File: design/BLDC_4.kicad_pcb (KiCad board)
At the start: 4 copper layers, 38.5 x 65 mm, 129 parts, among them K1 SERVO, P1 HALL/Encoder, P101 CANBUS, P2 SWD, P3 PWR_COMM, P4 IN+, P5 IN-, P6 MOTOR1, P7 MOTOR2, P9 MOTOR3, Q1 IRFS7530, Q2 IRFS7530, Q3 IRFS7530, Q4 IRFS7530, Q5 IRFS7530, Q6 IRFS7530, U1 STM32F40X_LQFP64, U2 TC2117, U3 DRV8302, U401 SN65HVD232, X1 MINI-USB-SHIELD-32005-201, X2 8MHz 10ppm

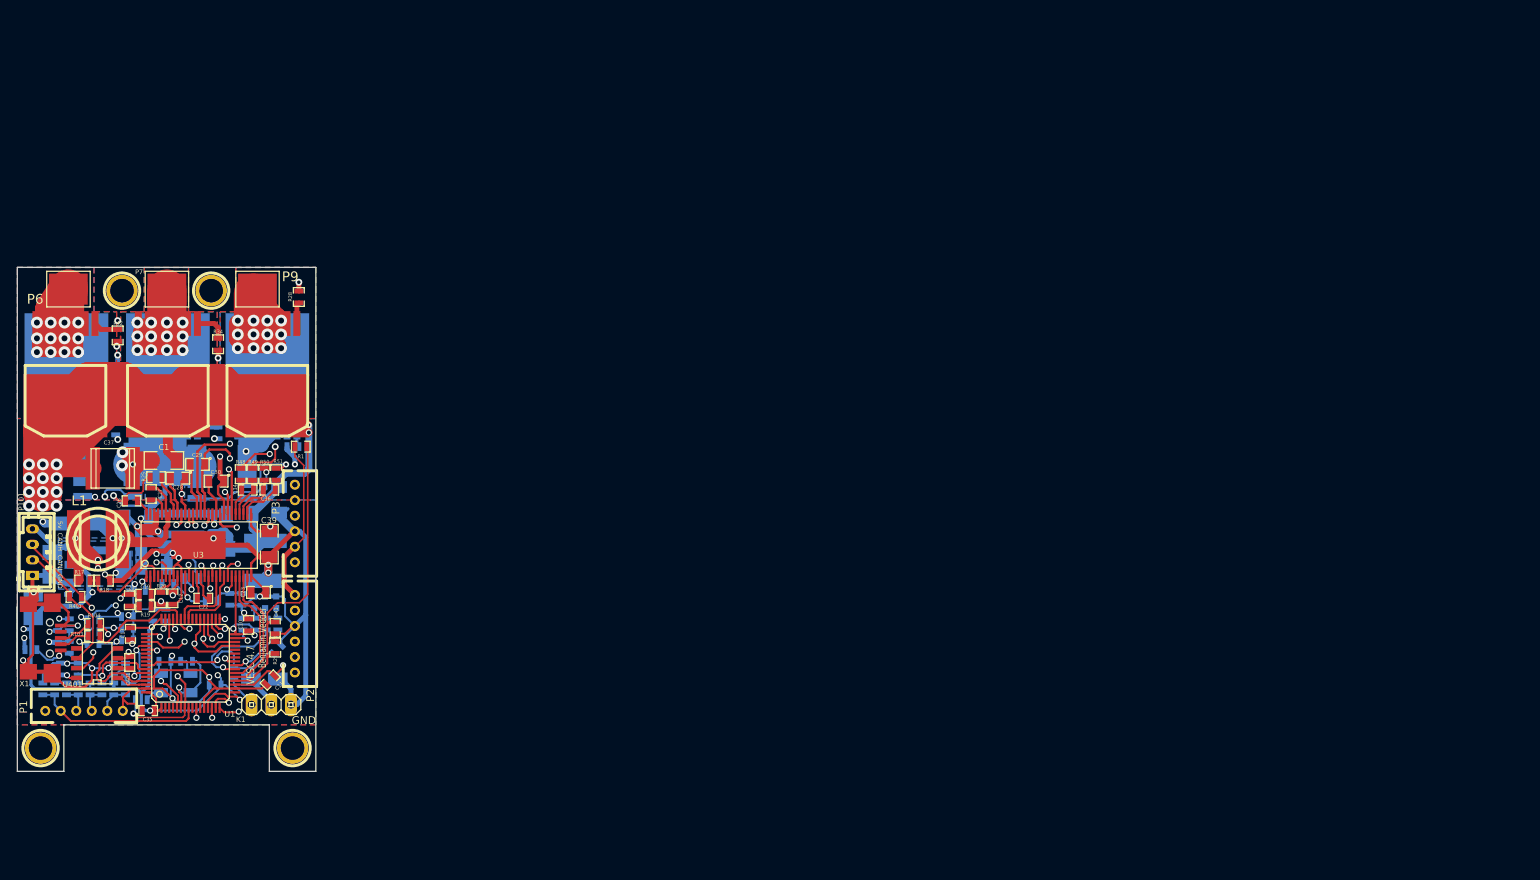
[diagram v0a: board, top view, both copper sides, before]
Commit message: Generated first netlist and started working with pcbnew.
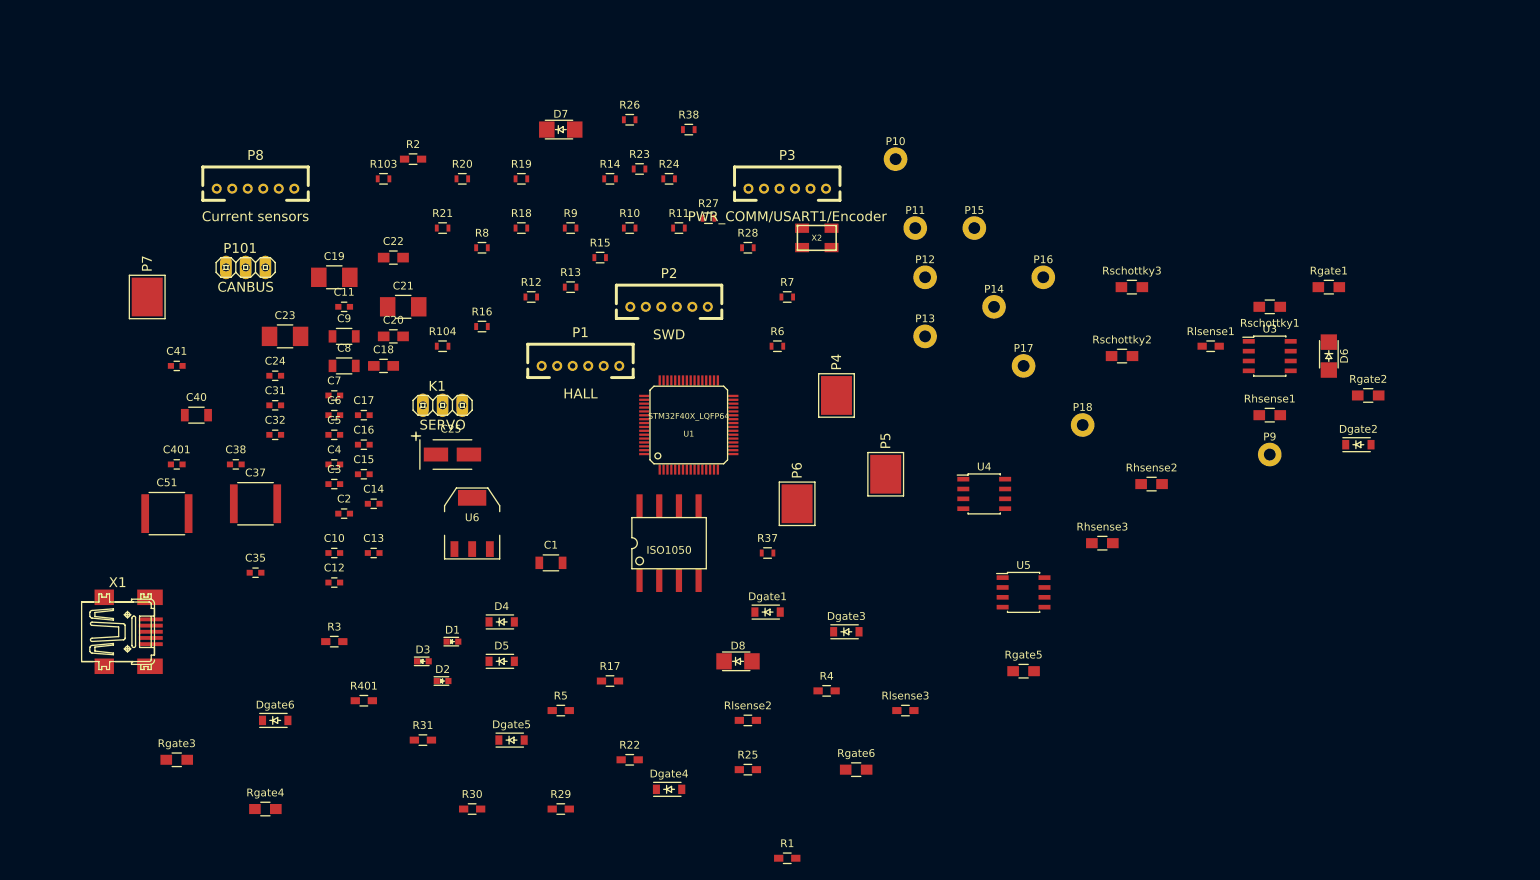
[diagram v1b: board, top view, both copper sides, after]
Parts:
- removed 1PIN (x2): P***, 1pin
- removed 1PIN (x2): P***, Connect:1pin
- removed C26: 15n, SMD_Packages:SMD-0603_c
- removed C27: 100n, SMD_Packages:SMD-0603_c
- removed C28, C29, C30: 220n, SMD_Packages:SMD-0805
- removed C33: 100u, w_smd_cap:c_tant_B
- removed C34, C36: 2.2n, SMD_Packages:SMD-0603_c
- removed C39, C43, C44, C49: 10u,50V, SMD_Packages:SMD-1206
- removed C52: 2.2u, SMD_Packages:SMD-0603_c
- removed G***: oshw_silkscreen-back_3mm, oshw_silkscreen-back_3mm
- removed L1: 22u, w_smd_inductors:inductor_smd_8x5mm
- removed Q1, Q2, Q3, Q4, Q5, Q6: IRFS7530, CRF1:D2PAK-7-GDS
- removed R32, R36, R46: 39k, SMD_Packages:SMD-0603_r
- removed R33: 2k2, SMD_Packages:SMD-0603_r
- removed R34, R35, R42, R43: 4R7, SMD_Packages:SMD-0603_r
- removed R402: 10k, SMD_Packages:SMD-0603_r
- removed R48, R49, R50, R51: 100R, SMD_Packages:SMD-0603_r
- removed R53, R54: SHUNT, CRF1:WSLP2726
- removed U401: SN65HVD232, SMD_Packages:SOIC-8-W
- added D6: D_Schottky, FootprintsBLDC:DO-214AC_SOD-123, F.Cu at (247.7, 91.4)
- added D7: D_Schottky, FootprintsBLDC:DO-214AC_SOD-123, F.Cu at (148.6, 62.2)
- added D8: D_Schottky, FootprintsBLDC:DO-214AC_SOD-123, F.Cu at (171.4, 130.8)
- added Dgate1: D, Diodes_SMD:SOD-123, F.Cu at (175.3, 124.5)
- added Dgate2: D, Diodes_SMD:SOD-123, F.Cu at (251.5, 102.9)
- added Dgate3: D, Diodes_SMD:SOD-123, F.Cu at (185.4, 127.0)
- added Dgate4: D, Diodes_SMD:SOD-123, F.Cu at (162.6, 147.3)
- added Dgate5: D, Diodes_SMD:SOD-123, F.Cu at (142.2, 141.0)
- added Dgate6: D, Diodes_SMD:SOD-123, F.Cu at (111.8, 138.4)
- added P10: CONN_DRV, FootprintsBLDC:PAD_DRV, F.Cu at (191.8, 66.0)
- added P11: CONN_DRV, FootprintsBLDC:PAD_DRV, F.Cu at (194.3, 74.9)
- added P12: CONN_DRV, FootprintsBLDC:PAD_DRV, F.Cu at (195.6, 81.3)
- added P13: CONN_DRV, FootprintsBLDC:PAD_DRV, F.Cu at (195.6, 88.9)
- added P14: CONN_DRV, FootprintsBLDC:PAD_DRV, F.Cu at (204.5, 85.1)
- added P15: CONN_DRV, FootprintsBLDC:PAD_DRV, F.Cu at (201.9, 74.9)
- added P16: CONN_DRV, FootprintsBLDC:PAD_DRV, F.Cu at (210.8, 81.3)
- added P17: CONN_DRV, FootprintsBLDC:PAD_DRV, F.Cu at (208.3, 92.7)
- added P18: CONN_DRV, FootprintsBLDC:PAD_DRV, F.Cu at (215.9, 100.3)
- added P8: Current sensors, CRF1:MICRO_JST_6, F.Cu at (109.2, 69.8)
- added R14: 100, Resistors_SMD:R_0603, F.Cu at (154.9, 68.6)
- added R31: R, Resistors_SMD:R_0603_HandSoldering, F.Cu at (130.8, 141.0)
- added Rgate1: 4.7, Resistors_SMD:R_0805_HandSoldering, F.Cu at (247.7, 82.5)
- added Rgate2: 4.7, Resistors_SMD:R_0805_HandSoldering, F.Cu at (252.7, 96.5)
- added Rgate3: 4.7, Resistors_SMD:R_0805_HandSoldering, F.Cu at (99.1, 143.5)
- added Rgate4: 4.7, Resistors_SMD:R_0805_HandSoldering, F.Cu at (110.5, 149.9)
- added Rgate5: 4.7, Resistors_SMD:R_0805_HandSoldering, F.Cu at (208.3, 132.1)
- added Rgate6: 4.7, Resistors_SMD:R_0805_HandSoldering, F.Cu at (186.7, 144.8)
- added Rhsense1: R, Resistors_SMD:R_0805_HandSoldering, F.Cu at (240.0, 99.1)
- added Rhsense2: R, Resistors_SMD:R_0805_HandSoldering, F.Cu at (224.8, 108.0)
- added Rhsense3: R, Resistors_SMD:R_0805_HandSoldering, F.Cu at (218.4, 115.6)
- added Rlsense1: R, Resistors_SMD:R_0603_HandSoldering, F.Cu at (232.4, 90.2)
- added Rlsense2: R, Resistors_SMD:R_0603_HandSoldering, F.Cu at (172.7, 138.4)
- added Rlsense3: R, Resistors_SMD:R_0603_HandSoldering, F.Cu at (193.0, 137.2)
- added Rschottky1: 2.7, Resistors_SMD:R_0805_HandSoldering, F.Cu at (240.0, 85.1)
- added Rschottky2: 2.7, Resistors_SMD:R_0805_HandSoldering, F.Cu at (221.0, 91.4)
- added Rschottky3: 2.7, Resistors_SMD:R_0805_HandSoldering, F.Cu at (222.2, 82.5)
- added U4: IRS2184, Housings_SOIC:SOIC-8_3.9x4.9mm_Pitch1.27mm, F.Cu at (203.2, 109.2)
- added U5: IRS2184, Housings_SOIC:SOIC-8_3.9x4.9mm_Pitch1.27mm, F.Cu at (208.3, 121.9)
- added U6: NCP1117ST33T3G, TO_SOT_Packages_SMD:SOT-223, F.Cu at (137.2, 113.0)
- C1: footprint SMD_Packages:SMD-1206 -> Capacitors_SMD:C_1206
- C10, C11, C12, C13, C35, C41: footprint SMD_Packages:SMD-0603_c -> Capacitors_SMD:C_0603
- C14, C15, C16, C17, C2, C24, C3, C31, C32, C38, C4, C5, C6, C7: footprint SMD_Packages:SMD-0603_c -> Capacitors_SMD:C_0603; moved to F.Cu
- C18: value 2.2u -> 0.47uF; footprint SMD_Packages:SMD-0805 -> Capacitors_SMD:C_0805_HandSoldering; moved to F.Cu
- C19: value 120p -> 1uF; footprint SMD_Packages:SMD-0603_c -> Capacitors_SMD:C_1210_HandSoldering
- C20: value 2.2u -> 0.47uF; footprint SMD_Packages:SMD-0603_c -> Capacitors_SMD:C_0805_HandSoldering; moved to F.Cu
- C21: value 6.8n -> 1uF; footprint SMD_Packages:SMD-0603_c -> Capacitors_SMD:C_1210_HandSoldering
- C22: value 22n -> 0.47uF; footprint SMD_Packages:SMD-0603_c -> Capacitors_SMD:C_0805_HandSoldering
- C23: value 2.2u -> 1uF; footprint SMD_Packages:SMD-0805 -> Capacitors_SMD:C_1210_HandSoldering
- C25: footprint w_smd_cap:c_tant_B -> Capacitors_Tantalum_SMD:TantalC_SizeB_EIA-3528_HandSoldering; moved to F.Cu
- C37: footprint w_smd_cap:c_2220 -> Capacitors_SMD:C_2220
- C40, C8, C9: footprint SMD_Packages:SMD-1206 -> Capacitors_SMD:C_1206; moved to F.Cu
- C401: footprint SMD_Packages:SMD-0603 -> Capacitors_SMD:C_0603
- C51: footprint w_smd_cap:c_2220 -> Capacitors_SMD:C_2220; moved to F.Cu
- D1, D2, D3, P4, P5, X2: moved to F.Cu
- D4: value DIODESCH -> BAT46WH; footprint Diodes_SMD:Diode-SMA_Handsoldering -> Diodes_SMD:SOD-123; moved to F.Cu
- D5: value TVS 5V -> BAT46WH; footprint w_smd_diode:do214ac -> Diodes_SMD:SOD-123; moved to F.Cu
- P1: value HALL/Encoder -> HALL
- P101: footprint JST conn:b4b-ph-kl -> CRF1:pinhead-1X03
- P3: value PWR_COMM -> PWR_COMM/USART1/Encoder
- P6: value MOTOR1 -> CONN_DRV
- P7: value MOTOR2 -> CONN_DRV
- P9: value MOTOR3 -> CONN_DRV; footprint CRF1:1PAD_4x5mm -> FootprintsBLDC:PAD_DRV
- R1, R2, R401: footprint SMD_Packages:SMD-0603_r -> Resistors_SMD:R_0603_HandSoldering
- R10, R11, R12, R13, R37, R38, R7, R8, R9: footprint SMD_Packages:SMD-0603_r -> Resistors_SMD:R_0603; moved to F.Cu
- R103, R104: footprint SMD_Packages:SMD-0603_r -> Resistors_SMD:R_0603
- R15: value 330k -> 100; footprint SMD_Packages:SMD-0603_r -> Resistors_SMD:R_0603; moved to F.Cu
- R16: value 10k -> 100; footprint SMD_Packages:SMD-0603_r -> Resistors_SMD:R_0603; moved to F.Cu
- R17: value 18k -> 0R; footprint SMD_Packages:SMD-0603_r -> Resistors_SMD:R_0603_HandSoldering
- R18: value 3k3 -> 1k; footprint SMD_Packages:SMD-0603_r -> Resistors_SMD:R_0603
- R19: value 15k -> 1k; footprint SMD_Packages:SMD-0603_r -> Resistors_SMD:R_0603
- R20: value 10k -> 1k; footprint SMD_Packages:SMD-0603_r -> Resistors_SMD:R_0603
- R21: value 220k -> 1k; footprint SMD_Packages:SMD-0603_r -> Resistors_SMD:R_0603; moved to F.Cu
- R22, R3, R4, R5: footprint SMD_Packages:SMD-0603_r -> Resistors_SMD:R_0603_HandSoldering; moved to F.Cu
- R23: value 39k -> 1k; footprint SMD_Packages:SMD-0603_r -> Resistors_SMD:R_0603; moved to F.Cu
- R24: value 2k2 -> 1k; footprint SMD_Packages:SMD-0603_r -> Resistors_SMD:R_0603; moved to F.Cu
- R25: value 1M -> 0R/DNP; footprint SMD_Packages:SMD-0603_r -> Resistors_SMD:R_0603_HandSoldering
- R26: value 39k -> R; footprint SMD_Packages:SMD-0603_r -> Resistors_SMD:R_0603; moved to F.Cu
- R27: value 2k2 -> R; footprint SMD_Packages:SMD-0603_r -> Resistors_SMD:R_0603; moved to F.Cu
- R28: value 4R7 -> R; footprint SMD_Packages:SMD-0603_r -> Resistors_SMD:R_0603
- R29: value 4R7 -> R; footprint SMD_Packages:SMD-0603_r -> Resistors_SMD:R_0603_HandSoldering; moved to F.Cu
- R30: value 39k -> R; footprint SMD_Packages:SMD-0603_r -> Resistors_SMD:R_0603_HandSoldering; moved to F.Cu
- R6: value 0R -> 10k; footprint SMD_Packages:SMD-0603_r -> Resistors_SMD:R_0603; moved to F.Cu
- U2: value TC2117 -> ISO1050; footprint SMD_Packages:SOT-223 -> CRF1:PDSO-G8; moved to F.Cu
- U3: value DRV8302 -> IRS2184; footprint CRF1:TSSOP-56-PP -> Housings_SOIC:SOIC-8_3.9x4.9mm_Pitch1.27mm
- X1: footprint Mrk Industries:USB-UX60R-MB-5ST -> CRF1:con-cypressindustries-32005-201
- moved U3 140.3 mm to (240.0, 91.4)
- moved P9 132.3 mm to (240.0, 104.1), turned to 0 degrees
- moved R7 107.2 mm to (177.8, 83.8), turned to 0 degrees
- moved R6 103.9 mm to (176.5, 90.2), turned to 0 degrees
- moved P4 103.1 mm to (184.2, 96.5)
- moved X2 100.7 mm to (181.6, 76.2)
- moved P6 98.0 mm to (179.1, 110.5), turned to 0 degrees
- moved R4 97.8 mm to (182.9, 134.6), turned to 0 degrees
- moved R26 95.7 mm to (157.5, 61.0)
- moved R11 94.1 mm to (163.8, 74.9), turned to 0 degrees
- moved R23 93.4 mm to (158.8, 67.3)
- moved P5 93.0 mm to (190.5, 106.7)
- moved R24 91.7 mm to (162.6, 68.6), turned to 0 degrees
- moved R27 91.7 mm to (167.6, 73.7), turned to 0 degrees
- moved R10 88.1 mm to (157.5, 74.9), turned to 0 degrees
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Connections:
- C18 pad 1: Net-(C18-Pad1) -> V_SUPPLY
- C19 pad 1: GND -> Net-(C19-Pad1)
- C19 pad 2: Net-(C19-Pad2) -> /Half Bridge Driver U/VS
- C20 pad 1: GND -> V_SUPPLY
- C20 pad 2: Net-(C20-Pad2) -> GND
- C21 pad 1: GND -> Net-(C21-Pad1)
- C21 pad 2: Net-(C21-Pad2) -> /Half Bridge Driver V/VS
- C22 pad 1: Net-(C22-Pad1) -> V_SUPPLY
- C22 pad 2: Net-(C22-Pad2) -> GND
- C23 pad 1: GND -> Net-(C23-Pad1)
- C23 pad 2: Net-(C23-Pad2) -> /Half Bridge Driver W/VS
- C31 pad 2: VCC -> Net-(C31-Pad2)
- C35 pad 2: VCC -> Net-(C31-Pad2)
- D4 pad 1: GND -> V_SUPPLY
- D4 pad 2: Net-(C27-Pad1) -> Net-(D4-Pad2)
- D5 pad 1: GND -> V_SUPPLY
- D5 pad 2: +5V -> Net-(D5-Pad2)
- K1 pad 2: +5V -> Net-(D5-Pad2)
- P1 pad 1: +5V -> /Filters/TEMP_IN
- P1 pad 2: /Filters/TEMP_IN -> /Filters/HALL1_IN
- P1 pad 3: /Filters/HALL1_IN -> /Filters/HALL2_IN
- P1 pad 4: /Filters/HALL2_IN -> /Filters/HALL3_IN
- P1 pad 5: /Filters/HALL3_IN -> GND
- P1 pad 6: GND -> VCC
- P101 pad 1: GND -> /CAN bus transceiver/CANGND
- P2 pad 6: Net-(P2-Pad6) -> (no net)
- P3 pad 3: /MCU/ADC_EXT -> Net-(P3-Pad3)
- P3 pad 4: GND -> Net-(P3-Pad4)
- P3 pad 5: VCC -> GND
- P3 pad 6: +5V -> VCC
- P6 pad 1: /Mosfet driver/H3_VS -> /Half Bridge Driver U/HO
- P7 pad 1: /Mosfet driver/H2_VS -> /Half Bridge Driver U/VS
- P9 pad 1: /Mosfet driver/H1_VS -> /Half Bridge Driver U/LO
- R15 pad 1: Net-(C20-Pad2) -> /MCU/USART1_TX
- R15 pad 2: Net-(R15-Pad2) -> Net-(P3-Pad4)
- R16 pad 1: Net-(R15-Pad2) -> /MCU/ADC_EXT
- R16 pad 2: GND -> Net-(P8-Pad4)
- R17 pad 1: +5V -> VCC
- R17 pad 2: Net-(R17-Pad2) -> Net-(C31-Pad2)
- R18 pad 1: Net-(R17-Pad2) -> Net-(R18-Pad1)
- R18 pad 2: GND -> /Half Bridge Driver U/DRV_IN
- R19 pad 1: Net-(C21-Pad2) -> Net-(R19-Pad1)
- R19 pad 2: Net-(C19-Pad2) -> /Half Bridge Driver U/DRV_SD
- R20 pad 2: GND -> /Half Bridge Driver V/DRV_IN
- R21 pad 1: GND -> Net-(R21-Pad1)
- R21 pad 2: Net-(R21-Pad2) -> /Half Bridge Driver V/DRV_SD
- R23 pad 1: /Mosfet driver/H3_VS -> Net-(R23-Pad1)
- R23 pad 2: /MCU/SENS1 -> /Half Bridge Driver W/DRV_IN
- R24 pad 1: GND -> Net-(R24-Pad1)
- R24 pad 2: /MCU/SENS1 -> /Half Bridge Driver W/DRV_SD
- R25 pad 1: GND -> VCC
- R25 pad 2: Net-(R25-Pad2) -> /IF-Current/V_SUPPLY
- R26 pad 1: /Mosfet driver/H2_VS -> /MCU/CURR1
- R26 pad 2: /MCU/SENS2 -> /IF-Current/CURR1_IN
- R27 pad 1: GND -> /MCU/CURR2
- R27 pad 2: /MCU/SENS2 -> /IF-Current/CURR2_IN
- R28 pad 1: Net-(Q1-PadG) -> /MCU/CURR3
- R28 pad 2: /Mosfet driver/M_H1 -> /IF-Current/CURR3_IN
- R29 pad 1: Net-(Q2-PadG) -> /MCU/SENSY
- R29 pad 2: /Mosfet driver/M_L1 -> /MCU/SENS1
- R30 pad 1: /Mosfet driver/H1_LOW -> /MCU/SENSY
- R30 pad 2: Net-(Q2-PadG) -> /MCU/SENS2
- R6 pad 1: Net-(R6-Pad1) -> Net-(D4-Pad2)
- R6 pad 2: +5V -> GND
- U1 pad 11: Net-(U1-Pad11) -> (no net)
- U1 pad 13: VCC -> Net-(C31-Pad2)
- U1 pad 17: Net-(U1-Pad17) -> /MCU/SENSY
- U1 pad 2: Net-(U1-Pad2) -> (no net)
- U1 pad 20: /MCU/ADC_TEMP -> /MCU/CURR3
- U1 pad 21: /MCU/BR_SO2 -> /MCU/CURR2
- U1 pad 22: /MCU/BR_SO1 -> /MCU/CURR1
- U1 pad 26: Net-(U1-Pad26) -> (no net)
- U1 pad 27: Net-(U1-Pad27) -> (no net)
- U1 pad 28: Net-(U1-Pad28) -> (no net)
- U1 pad 3: Net-(U1-Pad3) -> (no net)
- U1 pad 33: /MCU/DC_CAL -> (no net)
- U1 pad 34: /MCU/L3 -> /Half Bridge Driver W/DRV_SD
- U1 pad 35: /MCU/L2 -> /Half Bridge Driver V/DRV_SD
- U1 pad 36: /MCU/L1 -> /Half Bridge Driver U/DRV_SD
- U1 pad 39: Net-(U1-Pad39) -> (no net)
- U1 pad 4: Net-(U1-Pad4) -> (no net)
- U1 pad 40: Net-(U1-Pad40) -> (no net)
- U1 pad 41: /MCU/H3 -> /Half Bridge Driver W/DRV_IN
- U1 pad 42: /MCU/H2 -> /Half Bridge Driver V/DRV_IN
- U1 pad 43: /MCU/H1 -> /Half Bridge Driver U/DRV_IN
- U1 pad 50: Net-(U1-Pad50) -> (no net)
- U1 pad 51: /MCU/EN_GATE -> /Filters/HALL3_OUT
- U1 pad 52: /Filters/HALL3_OUT -> /Filters/HALL2_OUT
- U1 pad 53: /MCU/FAULT -> /Filters/HALL1_OUT
- U1 pad 54: Net-(U1-Pad54) -> (no net)
- U1 pad 55: Net-(U1-Pad55) -> (no net)
- U1 pad 56: Net-(U1-Pad56) -> (no net)
- U1 pad 58: /Filters/HALL1_OUT -> /MCU/USART1_TX
- U1 pad 59: /Filters/HALL2_OUT -> /MCU/USART1_RX
- U1 pad 9: Net-(U1-Pad9) -> /MCU/ADC_TEMP
- U2 pad 1: GND -> VCC
- U2 pad 2: VCC -> /CAN bus transceiver/CAN_RX
- U2 pad 3: +5V -> /CAN bus transceiver/CAN_TX
- U3 pad 1: Net-(R21-Pad2) -> Net-(R18-Pad1)
- U3 pad 2: Net-(C19-Pad2) -> Net-(R19-Pad1)
- U3 pad 3: Net-(R17-Pad2) -> GND
- U3 pad 5: Net-(U3-Pad5) -> V_SUPPLY
- U3 pad 6: /MCU/FAULT -> /Half Bridge Driver U/VS
- U3 pad 7: Net-(R20-Pad1) -> Net-(Dgate1-Pad1)
- U3 pad 8: GND -> Net-(C19-Pad1)
- X1 pad 1: Net-(R6-Pad1) -> Net-(D4-Pad2)
- X1 pad 4: Net-(X1-Pad4) -> (no net)
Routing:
- net GND: track 415.0 -> 0.00 mm, vias 31 -> 0
- net V_SUPPLY: track 264.9 -> 0.00 mm, vias 18 -> 0
- net VCC: track 188.9 -> 0.00 mm, vias 12 -> 0
- net /Mosfet driver/H3_VS: track 150.9 -> 0.00 mm, vias 15 -> 0
- net /Mosfet driver/H1_VS: track 147.1 -> 0.00 mm, vias 14 -> 0
- net /Mosfet driver/H2_VS: track 138.5 -> 0.00 mm, vias 14 -> 0
- net +5V: track 116.4 -> 0.00 mm, vias 4 -> 0
- net /Mosfet driver/H3_LOW: track 89.8 -> 0.00 mm, vias 2 -> 0
- net /Mosfet driver/H1_LOW: track 57.6 -> 0.00 mm, vias 2 -> 0
- net /Mosfet driver/M_H1: track 49.4 -> 0.00 mm, vias 2 -> 0
- net /MCU/TX_SDA: track 41.5 -> 0.00 mm, vias 1 -> 0
- net /Mosfet driver/SH1_B: track 40.8 -> 0.00 mm, vias 2 -> 0
- net /Mosfet driver/M_H3: track 40.8 -> 0.00 mm, vias 2 -> 0
- net /MCU/ADC_TEMP: track 39.2 -> 0.00 mm
- net /MCU/RX_SCL: track 39.1 -> 0.00 mm, vias 1 -> 0
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- removed copper zone on B.Cu, net /Mosfet driver/H1_VS
- removed copper zone on F.Cu, net /Mosfet driver/H1_VS
- removed copper zone on GND, net /Mosfet driver/H1_VS
- removed copper zone on Power, net /Mosfet driver/H1_VS
- removed copper zone on B.Cu, net /Mosfet driver/H2_VS
- removed copper zone on F.Cu, net /Mosfet driver/H2_VS
- removed copper zone on GND, net /Mosfet driver/H2_VS
- removed copper zone on Power, net /Mosfet driver/H2_VS
- removed copper zone on B.Cu, net /Mosfet driver/H3_VS
- removed copper zone on F.Cu, net /Mosfet driver/H3_VS
- removed copper zone on GND, net /Mosfet driver/H3_VS
- removed copper zone on Power, net /Mosfet driver/H3_VS
- removed copper zone on B.Cu, net GND
- removed copper zone on F.Cu, net GND
- removed copper zone on GND, net GND
- removed copper zone on B.Cu, net VCC
- removed copper zone on Power, net VCC
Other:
- board outline removed
- copper layers 4 -> 2
- net class Default: clearance 0.1778 -> 0.2; trace_width 0.2032 -> 0.25; via_dia 0.8 -> 0.6; via_drill 0.5 -> 0.4
- rule trace_clearance: 0.1778 -> 0.2
- rule trace_min: 0.2032 -> 0.2
- rule via_min_drill: 0.5 -> 0.3
- rule via_min_size: 0.8 -> 0.4
- board text removed: "3.3V"
- board text removed: "3.3v"
- board text removed: "5v"
- board text removed: "ADC"
- board text removed: "Benjamin Vedder"
- board text removed: "CANH"
- board text removed: "CANL"
- board text removed: "CLK"
- board text removed: "DIO"
- board text removed: "GND"
- board text removed: "H1"
- board text removed: "H2"
- board text removed: "H3"
- board text removed: "Mrk Industries"
- board text removed: "RST"
- board text removed: "TEMP"
- board text removed: "VESC 4.7"
- board text removed: "vedder.se"
